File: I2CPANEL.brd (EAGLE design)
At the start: 54 x 83 mm, 47 parts, among them IC1 ATMEGA32U4-QFN

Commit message: Schematic and routing for v1.0 release
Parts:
- removed C1: 100nF 0603, freetronics-master-v1.1:0603
- removed C3, C4: 1uF 0603, freetronics-master-v1.1:0603
- removed C5, C6: 15pF 0603, freetronics-master-v1.1:0603
- removed F1: 500mA PTC 1812, rcl:L1812
- removed IC1: ATMEGA32U4-QFN, freetronics-jon:QFN-44N
- removed ICSP: ICSP, pinhead:2X03
- removed LED2: RED, freetronics-jon:LED-0603
- removed LED3: GREEN, freetronics-jon:LED-0603
- removed R1, R6: 22R, freetronics-jon:0603
- removed R18: 5.1K, freetronics-original:0603
- removed R2: 10K 0603, freetronics-master-v1.1:0603
- removed R4, R5: 1K, freetronics-jon:0603
- removed S10: 10, freetronics-original:TACTILE-PTH
- removed S11: 11, freetronics-original:TACTILE-PTH
- removed S12: 12, freetronics-original:TACTILE-PTH
- removed S13: 13, freetronics-original:TACTILE-PTH
- removed S14: 14, freetronics-original:TACTILE-PTH
- removed S15: 15, freetronics-original:TACTILE-PTH
- removed S16: 16, freetronics-original:TACTILE-PTH
- removed S17: 17, freetronics-original:TACTILE-PTH
- removed S18: 18, freetronics-original:TACTILE-PTH
- removed S19: 19, freetronics-original:TACTILE-PTH
- removed S20: 20, freetronics-original:TACTILE-PTH
- removed S21: RESET, freetronics-jon:TACTILE_SWITCH_SMD_2PIN_TINY
- removed S22: HWB, freetronics-jon:TACTILE_SWITCH_SMD_2PIN_TINY
- removed S7: 7, freetronics-original:TACTILE-PTH
- removed S8: 8, freetronics-original:TACTILE-PTH
- removed S9: 9, freetronics-original:TACTILE-PTH
- removed U$15: USB-C, freetronics-jon:USB-C-U52A
- removed XTL1: 16MHz, freetronics-jon:CRYSTAL-SMD-3X2
- removed Z1, Z2: PGB1010603, freetronics-master-v1.1:0603
- added IC2: MCP23017SO, microchip:SO28W
- added JP1: M100.1, freetronics-original:1X10
- added JP3: OLED, freetronics-jon:1X04
- added R27, R28: 4K7, freetronics-master-v1:0603
- added R29, R30, R31: 10K, freetronics-master-v1:0603
- added SJ2, SJ3, SJ4, SJ5: (no value), freetronics-jon:SJ
- C2: value 100nF 0603 -> 1uF
- SJ1: value HWB -> (none)
- moved LED1 99.4 mm to (72.5, 4.00)
- moved JP2 97.4 mm to (92.0, 19.0), flipped to the bottom
- moved R3 94.3 mm to (70.5, 4.00), turned to 90 degrees
- moved C2 87.0 mm to (88.0, 8.00)
- moved SJ1 67.3 mm to (56.0, 26.0), turned to 90 degrees
- moved S1 51.0 mm to (44.0, 15.0), flipped to the bottom
- moved S4 46.6 mm to (32.0, 8.00), flipped to the bottom
- moved S2 38.0 mm to (20.0, 15.0), flipped to the bottom
- moved S6 36.1 mm to (9.00, 8.00), flipped to the bottom
- moved S3 31.0 mm to (32.0, 22.0), flipped to the bottom
- moved S5 20.0 mm to (9.00, 22.0), flipped to the bottom
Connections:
- removed net 3V3: C4.2, IC1.6
- removed net 5V: C2.1, C3.1, F1.2, IC1.14, IC1.2, IC1.24, IC1.34, IC1.44, IC1.7, ICSP.2, JP2.3, R2.2, R3.2, R4.2, R5.2
- removed net A0: IC1.36
- removed net A1: IC1.37
- removed net A2: IC1.38
- removed net A3: IC1.39
- removed net A4: IC1.40
- removed net A5: IC1.41
- removed net AREF: C1.1, IC1.42
- removed net COL0: IC1.25, S1.1, S1.2, S13.1, S13.2, S17.1, S17.2, S5.1, S5.2, S9.1, S9.2
- removed net COL1: IC1.31, S10.1, S10.2, S14.1, S14.2, S18.1, S18.2, S2.1, S2.2, S6.1, S6.2
- removed net COL2: IC1.20, S11.1, S11.2, S15.1, S15.2, S19.1, S19.2, S3.1, S3.2, S7.1, S7.2
- removed net COL3: IC1.21, S12.1, S12.2, S16.1, S16.2, S20.1, S20.2, S4.1, S4.2, S8.1, S8.2
- removed net D+: R6.1, U$15.A6, U$15.B6, Z2.2
- removed net D-: R1.1, U$15.A7, U$15.B7, Z1.2
- removed net D11: IC1.12
- removed net D13: IC1.32
- removed net D2_SDA: IC1.19, JP2.1
- removed net D3_SCL: IC1.18, JP2.2
- removed net D7_AIN0: IC1.1
- removed net HWB: IC1.33, S22.1, SJ1.1
- removed net MISO: IC1.11, ICSP.1
- removed net MOSI: IC1.10, ICSP.4
- removed net N$11: C5.2, IC1.17, XTL1.3
- removed net N$12: C6.2, IC1.16, XTL1.1
- removed net N$67: R18.2, U$15.A5, U$15.B5
- removed net RD+: IC1.4, R6.2
- removed net RD-: IC1.3, R1.2
- removed net RESET: IC1.13, ICSP.5, R2.1, S21.2
- removed net ROW0: IC1.27, S1.3, S1.4, S2.3, S2.4, S3.3, S3.4, S4.3, S4.4
- removed net ROW1: IC1.26, S5.3, S5.4, S6.3, S6.4, S7.3, S7.4, S8.3, S8.4
- removed net ROW2: IC1.28, S10.3, S10.4, S11.3, S11.4, S12.3, S12.4, S9.3, S9.4
- removed net ROW3: IC1.29, S13.3, S13.4, S14.3, S14.4, S15.3, S15.4, S16.3, S16.4
- removed net ROW4: IC1.30, S17.3, S17.4, S18.3, S18.4, S19.3, S19.4, S20.3, S20.4
- removed net RXLED_SS: IC1.8, LED3.C
- removed net SCK: IC1.9, ICSP.3
- removed net TX_LED: IC1.22, LED2.C
- removed net USB+: F1.1, U$15.A4, U$15.A9, U$15.B4, U$15.B9
- new net ADDR0: IC2.15, R29.2, SJ1.1
- new net ADDR1: IC2.16, R30.2, SJ2.1
- new net ADDR2: IC2.17, R31.2, SJ3.1
- new net GPA1: IC2.22, S1.1, S1.2
- new net GPA2: IC2.23, S2.1, S2.2
- new net GPA3: IC2.24, S3.1, S3.2
- new net GPA4: IC2.25, S4.1, S4.2
- new net GPA5: IC2.26, S5.1, S5.2
- new net GPA6: IC2.27, S6.1, S6.2
- new net N$1: IC2.1, JP1.1
- new net N$2: IC2.2, JP1.2
- new net N$3: IC2.3, JP1.3
- new net N$4: IC2.4, JP1.4
- new net N$42: R27.2, SJ4.1
- new net N$43: R28.2, SJ5.1
- new net N$5: IC2.5, JP1.5
- new net N$9: IC2.8, JP1.8
- new net SCL: IC2.12, JP2.2, JP3.2, R27.1
- new net SDA: IC2.13, JP2.1, JP3.1, R28.1
- new net VCC: C2.1, IC2.18, IC2.9, JP1.9, JP2.3, JP3.3, R3.2, SJ1.2, SJ2.2, SJ3.2, SJ4.2, SJ5.2
- net GND: now also IC2.10, JP1.10, JP3.4, R29.1, R30.1, R31.1, S1.3, S1.4, S2.3, S2.4, S3.3, S3.4, S4.3, S4.4, S5.3, S5.4, S6.3, S6.4; no longer C1.2, C3.2, C4.1, C5.1, C6.1, IC1.15, IC1.23, IC1.35, IC1.43, IC1.5, IC1.TGND, ICSP.6, R18.1, S21.1, S22.2, SJ1.2, U$15.A1, U$15.A12, U$15.B1, U$15.B12, U$15.CASE1, U$15.CASE2, U$15.CASE3, U$15.CASE4, U$15.FIX1, U$15.FIX2, U$15.FIX3, U$15.FIX4, XTL1.2, XTL1.4, Z1.1, Z2.1
- net N$7: now also IC2.6, JP1.6; no longer LED2.A, R4.1
- net N$8: now also IC2.7, JP1.7; no longer LED3.A, R5.1
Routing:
- net ROW4: track 123.0 -> 0.00 mm
- net ROW3: track 111.5 -> 0.00 mm
- net 5V: track 111.1 -> 0.00 mm, vias 5 -> 0
- net ROW2: track 100.0 -> 0.00 mm
- net COL0: track 88.9 -> 0.00 mm, vias 1 -> 0
- net ROW1: track 88.6 -> 0.00 mm
- net COL1: track 86.0 -> 0.00 mm, vias 1 -> 0
- net ROW0: track 76.2 -> 0.00 mm, vias 1 -> 0
- net SDA: track 0.00 -> 68.0 mm, vias 0 -> 1
- net COL3: track 67.0 -> 0.00 mm
- net COL2: track 65.5 -> 0.00 mm
- net HWB: track 60.6 -> 0.00 mm, vias 2 -> 0
- net GPA5: track 0.00 -> 59.5 mm
- net SCL: track 0.00 -> 55.3 mm, vias 0 -> 1
- net GPA6: track 0.00 -> 53.0 mm
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- added copper zone on layer 1, net VCC
- removed copper zone on layer 1, net GND
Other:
- board size 54 x 83 mm -> 99 x 30 mm
- board text added: "0"
- board text added: "A0"
- board text added: "A1"
- board text added: "A2"
- board text added: "Copyright 2019 SuperHouse Automation Pty Ltd Released under the TAPR Open Hardware License www.tapr.org/OHL"
- board text added: "G"
- board text added: "GPA1"
- board text added: "GPA2"
- board text added: "GPA3"
- board text added: "GPA4"
- board text added: "GPA5"
- board text added: "GPA6"
- board text added: "GPB0-7"
- board text added: "I2C"
- board text added: "I2C Addresses: 0x20 MCP23017 0x3C 128x32 OLED"
- board text added: "I2C Control Panel"
- board text added: "Pullups"
- board text added: "SCL"
- board text added: "SDA"
- board text added: "V"
- board text added: "VIN"
- board text added: "VIN: 3.3-5V"
- board text added: "www.superhouse.tv/i2cpanel"
- board text removed: "10"
- board text removed: "11"
- board text removed: "12"
- board text removed: "13"
- board text removed: "14"
- board text removed: "15"
- board text removed: "16"
- board text removed: "17"
- board text removed: "18"
- board text removed: "19"
- board text removed: "20"
- board text removed: "8"
- board text removed: "9"
- board text removed: "Arduino Leonardo Compatible"
- board text removed: "Col0: D4 Col1: D5 Col2: D0 Col3: D1"
- board text removed: "Copyright 2018 SuperHouse Automation Pty Ltd Released under the TAPR Open Hardware License www.tapr.org/OHL"
- board text removed: "HWB"
- board text removed: "ICSP"
- board text removed: "LeoPad Mini"
- board text removed: "RST"
- board text removed: "Row0: D6 Row1: D12 Row2: D8 Row3: D9 Row4: D10"
- board text removed: "Rx"
- board text removed: "Tx"
- board text removed: "USB-C"
- board text removed: "www.superhouse.tv/lpmini"

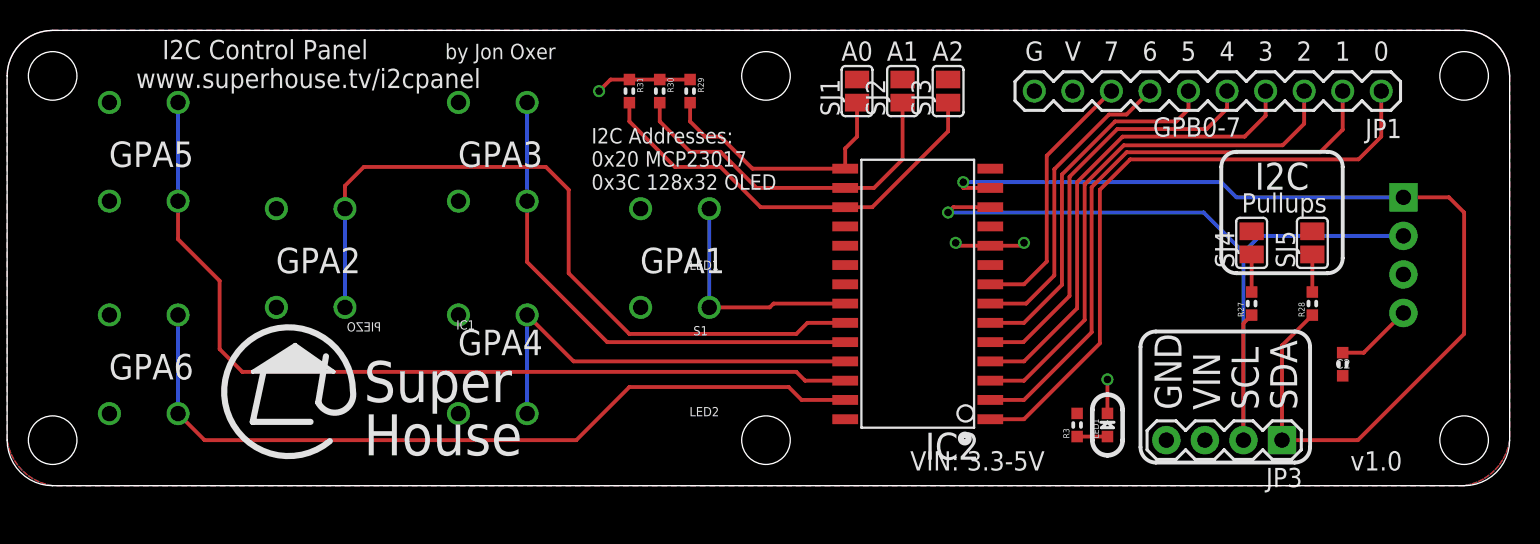
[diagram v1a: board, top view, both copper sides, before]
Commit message: Major rework to use 128x32 screen for v1.0 release
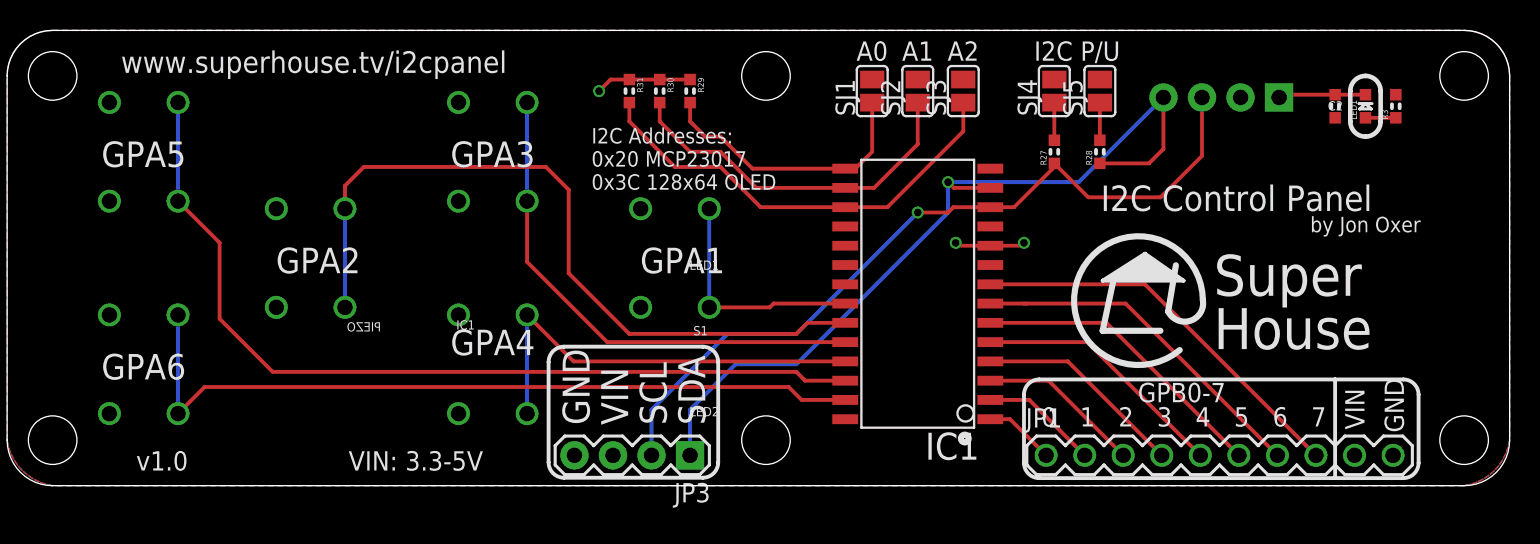
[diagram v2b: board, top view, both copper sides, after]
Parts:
- removed JP2: OLED, freetronics-jon:1X04
- added IC1: MCP23017SO, microchip:SO28W
- IC2: value MCP23017SO -> 128X64 OLED; device microchip:SO28W -> freetronics-jon:OLED-128X64
- moved JP3 39.0 mm to (45.0, 2.00)
- moved JP1 32.6 mm to (68.5, 2.00), turned to 0 degrees
- moved R3 29.7 mm to (91.5, 25.0)
- moved LED1 27.0 mm to (89.5, 25.0)
- moved IC2 20.2 mm to (80.0, 15.0), flipped to the bottom, turned to 0 degrees
- moved R28 17.2 mm to (72.0, 22.0)
- moved SJ5 17.2 mm to (72.0, 26.0)
- moved C2 17.0 mm to (87.5, 25.0)
- moved R27 16.4 mm to (69.0, 22.0)
- moved SJ4 16.4 mm to (69.0, 26.0)
- moved SJ1 1.00 mm to (57.0, 26.0)
- moved SJ2 1.00 mm to (60.0, 26.0)
- moved SJ3 1.00 mm to (63.0, 26.0)
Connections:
- net ADDR0: now also IC1.15; no longer IC2.15
- net ADDR1: now also IC1.16; no longer IC2.16
- net ADDR2: now also IC1.17; no longer IC2.17
- net GND: now also IC1.10, IC2.GND; no longer IC2.10, JP2.4
- net GPA1: now also IC1.22; no longer IC2.22
- net GPA2: now also IC1.23; no longer IC2.23
- net GPA3: now also IC1.24; no longer IC2.24
- net GPA4: now also IC1.25; no longer IC2.25
- net GPA5: now also IC1.26; no longer IC2.26
- net GPA6: now also IC1.27; no longer IC2.27
- net N$1: now also IC1.1; no longer IC2.1
- net N$2: now also IC1.2; no longer IC2.2
- net N$3: now also IC1.3; no longer IC2.3
- net N$4: now also IC1.4; no longer IC2.4
- net N$5: now also IC1.5; no longer IC2.5
- net N$7: now also IC1.6; no longer IC2.6
- net N$8: now also IC1.7; no longer IC2.7
- net N$9: now also IC1.8; no longer IC2.8
- net SCL: now also IC1.12, IC2.SCL; no longer IC2.12, JP2.2
- net SDA: now also IC1.13, IC2.SDA; no longer IC2.13, JP2.1
- net VCC: now also IC1.18, IC1.9, IC2.VCC; no longer IC2.18, IC2.9, JP2.3
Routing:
- net N$1: track 42.4 -> 4.67 mm
- net N$2: track 38.7 -> 7.73 mm
- net N$3: track 35.1 -> 10.8 mm
- net N$4: track 31.3 -> 13.9 mm
- net SDA: track 68.0 -> 54.8 mm
- net N$5: track 27.7 -> 16.9 mm
- net N$9: track 17.3 -> 26.1 mm
- net N$7: track 24.3 -> 20.0 mm
- net SCL: track 55.3 -> 52.0 mm
- net N$8: track 20.4 -> 23.1 mm
- net GND: track 18.3 -> 16.7 mm, vias 4 -> 3
- net GPA6: track 53.0 -> 51.5 mm
- net GPA5: track 59.5 -> 58.3 mm
- net ADDR2: track 28.5 -> 29.5 mm
- net ADDR0: track 17.4 -> 18.2 mm
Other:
- board text added: "I2C Addresses: 0x20 MCP23017 0x3C 128x64 OLED"
- board text added: "I2C P/U"
- board text removed: "5V"
- board text removed: "D2/SDA"
- board text removed: "D3/SCL"
- board text removed: "G"
- board text removed: "I2C"
- board text removed: "I2C Addresses: 0x20 MCP23017 0x3C 128x32 OLED"
- board text removed: "Pullups"
- board text removed: "V"

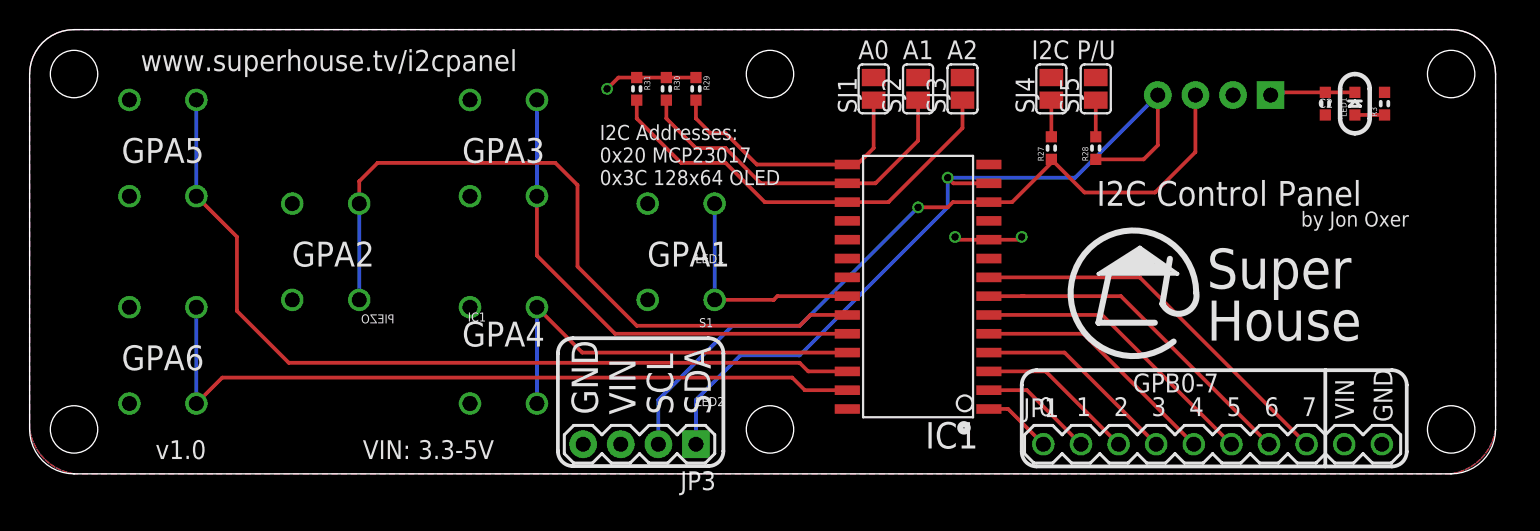
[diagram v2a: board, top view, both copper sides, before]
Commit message: Added mechanical dimensions
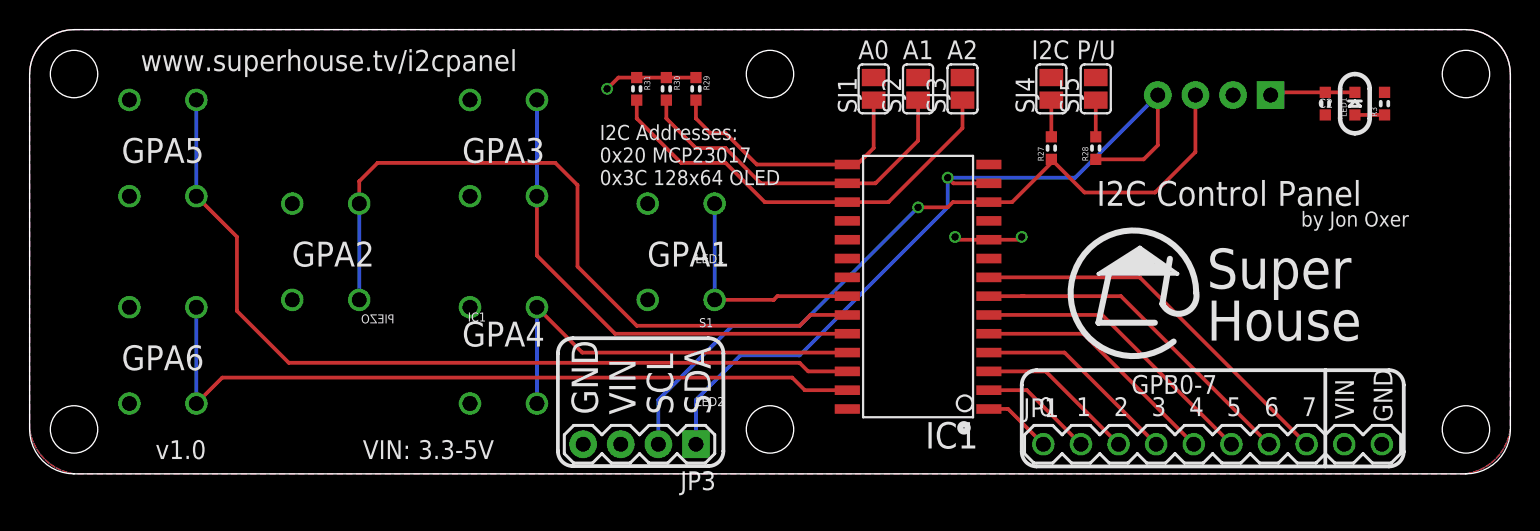
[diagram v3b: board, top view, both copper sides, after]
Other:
- board size 99 x 30 mm -> 100 x 30 mm
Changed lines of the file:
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@@
 <setting verticaltext="up"/>
 </settings>
-<grid distance="0.5" unitdist="mm" unit="mm" style="dots" multiple="1" display="yes" altdistance="0.001" altunitdist="inch" altunit="inch"/>
+<grid distance="1" unitdist="mm" unit="mm" style="dots" multiple="1" display="yes" altdistance="0.001" altunitdist="inch" altunit="inch"/>
 <layers>
 <layer number="1" name="Top" color="4" fill="1" visible="yes" active="yes"/>
@@
 <layer number="45" name="Holes" color="7" fill="1" visible="yes" active="yes"/>
 <layer number="46" name="Milling" color="3" fill="1" visible="no" active="yes"/>
-<layer number="47" name="Measures" color="7" fill="1" visible="no" active="yes"/>
+<layer number="47" name="Measures" color="7" fill="1" visible="yes" active="yes"/>
 <layer number="48" name="Document" color="7" fill="1" visible="no" active="yes"/>
 <layer number="49" name="Reference" color="7" fill="1" visible="no" active="yes"/>
@@
 <board>
 <plain>
-<wire x1="3" y1="0" x2="96" y2="0" width="0" layer="20"/>
-<wire x1="99" y1="3" x2="99" y2="27" width="0" layer="20"/>
-<wire x1="96" y1="30" x2="3" y2="30" width="0" layer="20"/>
+<wire x1="3" y1="0" x2="97" y2="0" width="0" layer="20"/>
+<wire x1="100" y1="3" x2="100" y2="27" width="0" layer="20"/>
+<wire x1="97" y1="30" x2="3" y2="30" width="0" layer="20"/>
 <wire x1="0" y1="3" x2="3" y2="0" width="0" layer="20" curve="90"/>
 <wire x1="0" y1="3" x2="0" y2="27" width="0" layer="20"/>
 <wire x1="0" y1="27" x2="3" y2="30" width="0" layer="20" curve="-90"/>
-<wire x1="96" y1="30" x2="99" y2="27" width="0" layer="20" curve="-90"/>
-<wire x1="96" y1="0" x2="99" y2="3" width="0" layer="20" curve="90"/>
+<wire x1="97" y1="30" x2="100" y2="27" width="0" layer="20" curve="-90"/>
+<wire x1="97" y1="0" x2="100" y2="3" width="0" layer="20" curve="90"/>
 <circle x="63.1" y="3.1064" radius="0.254" width="0.4064" layer="21"/>
 <text x="7.5" y="27.2" size="1.4224" layer="21" font="vector" ratio="17">www.superhouse.tv/i2cpanel</text>
@@
 <text x="8.5" y="1" size="1.27" layer="21" font="vector" ratio="15">v1.0</text>
 <hole x="3" y="27" drill="3.2"/>
-<hole x="96" y="27" drill="3.2"/>
+<hole x="97" y="27" drill="3.2"/>
 <text x="81" y="18.1" size="1.6764" layer="21" font="vector" ratio="18" align="bottom-center">I2C Control Panel</text>
 <hole x="3" y="3" drill="3.2"/>
-<hole x="96" y="3" drill="3.2"/>
+<hole x="97" y="3" drill="3.2"/>
 <text x="24.5" y="14" size="2.54" layer="22" font="vector" ratio="15" rot="MR0" align="bottom-center">2</text>
 <text x="48.5" y="14" size="2.54" layer="22" font="vector" ratio="15" rot="MR0" align="bottom-center">1</text>
@@
 0x20 MCP23017
 0x3C 128x64 OLED</text>
-<text x="74.5" y="5.5" size="1.27" layer="21" font="vector" ratio="15">GPB0-7</text>
+<text x="74.4" y="5.4" size="1.27" layer="21" font="vector" ratio="15">GPB0-7</text>
 <text x="22.5" y="1" size="1.27" layer="21" font="vector" ratio="15">VIN: 3.3-5V</text>
 <text x="70.5" y="28" size="1.27" layer="21" font="vector" ratio="16" align="bottom-center">I2C P/U</text>
 <wire x1="68" y1="7" x2="67" y2="6" width="0.254" layer="21" curve="90"/>
 <wire x1="68" y1="7" x2="87.5" y2="7" width="0.254" layer="21"/>
-<wire x1="87.5" y1="7" x2="92" y2="7" width="0.254" layer="21"/>
-<wire x1="92" y1="7" x2="93" y2="6" width="0.254" layer="21" curve="-90"/>
+<wire x1="87.5" y1="7" x2="91.8" y2="7" width="0.254" layer="21"/>
+<wire x1="91.8" y1="7" x2="92.8" y2="6" width="0.254" layer="21" curve="-90"/>
 <wire x1="87.5" y1="0.5" x2="87.5" y2="7" width="0.254" layer="21"/>
-<wire x1="68" y1="0.5" x2="92" y2="0.5" width="0.254" layer="21"/>
+<wire x1="68" y1="0.5" x2="91.8" y2="0.5" width="0.254" layer="21"/>
 <wire x1="68" y1="0.5" x2="67" y2="1.5" width="0.254" layer="21" curve="-90"/>
 <wire x1="67" y1="1.5" x2="67" y2="6" width="0.254" layer="21"/>
-<wire x1="92" y1="0.5" x2="93" y2="1.5" width="0.254" layer="21" curve="90"/>
-<wire x1="93" y1="1.5" x2="93" y2="6" width="0.254" layer="21"/>
+<wire x1="91.8" y1="0.5" x2="92.8" y2="1.5" width="0.254" layer="21" curve="90"/>
+<wire x1="92.8" y1="1.5" x2="92.8" y2="6" width="0.254" layer="21"/>
+<dimension x1="0" y1="30" x2="100" y2="30" x3="50" y3="37" textsize="1.778" layer="47" precision="0" visible="yes"/>
+<dimension x1="100" y1="0" x2="100" y2="30" x3="109" y3="15" textsize="1.778" layer="47" precision="0" visible="yes"/>
+<dimension x1="99" y1="27" x2="99" y2="3" x3="106" y3="15" textsize="1.778" layer="47" dtype="diameter" precision="0" visible="yes"/>
+<dimension x1="3" y1="29" x2="50" y2="29" x3="26.5" y3="32" textsize="1.778" layer="47" dtype="horizontal" precision="0" visible="yes"/>
+<dimension x1="50" y1="29" x2="97" y2="29" x3="73.5" y3="32" textsize="1.778" layer="47" dtype="horizontal" precision="0" visible="yes"/>
+<dimension x1="3" y1="29" x2="0" y2="34" x3="1.5" y3="34" textsize="1.778" layer="47" dtype="horizontal" precision="0" visible="yes"/>
+<dimension x1="99" y1="3" x2="102" y2="0" x3="103" y3="1.5" textsize="1.778" layer="47" dtype="vertical" precision="0" visible="yes"/>
+<dimension x1="93" y1="9" x2="93" y2="21" x3="97" y3="15" textsize="1.778" layer="47" dtype="vertical" precision="0" visible="yes"/>
+<dimension x1="68" y1="-1" x2="92" y2="-1" x3="80" y3="-3" textsize="1.778" layer="47" dtype="horizontal" precision="0" visible="yes"/>
+<dimension x1="68" y1="-1" x2="44" y2="-1" x3="56" y3="-3" textsize="1.778" layer="47" dtype="horizontal" precision="0" visible="yes"/>
+<dimension x1="44" y1="-1" x2="32" y2="-1" x3="38" y3="-3" textsize="1.778" layer="47" dtype="horizontal" precision="0" visible="yes"/>
+<dimension x1="32" y1="-1" x2="20" y2="-1" x3="26" y3="-3" textsize="1.778" layer="47" dtype="horizontal" precision="0" visible="yes"/>
+<dimension x1="20" y1="-1" x2="9" y2="-1" x3="14.5" y3="-3" textsize="1.778" layer="47" dtype="horizontal" precision="0" visible="yes"/>
+<dimension x1="9" y1="-1" x2="0" y2="-1" x3="4.5" y3="-3" textsize="1.778" layer="47" dtype="horizontal" precision="0" visible="yes"/>
+<dimension x1="92" y1="-1" x2="100" y2="-1" x3="96" y3="-3" textsize="1.778" layer="47" dtype="horizontal" precision="0" visible="yes"/>
+<dimension x1="5" y1="8" x2="5" y2="22" x3="-2" y3="15" textsize="1.778" layer="47" dtype="vertical" precision="0" visible="yes"/>
+<dimension x1="-1" y1="0" x2="-1" y2="8" x3="-2" y3="4" textsize="1.778" layer="47" dtype="vertical" precision="0" visible="yes"/>
+<dimension x1="-1" y1="22" x2="-1" y2="30" x3="-2" y3="26" textsize="1.778" layer="47" dtype="vertical" precision="0" visible="yes"/>
 </plain>
 <attributes>
@@
 <vertex x="0" y="27" curve="-90"/>
 <vertex x="3" y="30"/>
-<vertex x="96" y="30" curve="-90"/>
-<vertex x="99" y="27"/>
-<vertex x="99" y="3" curve="-73.73763"/>
-<vertex x="96" y="0"/>
+<vertex x="97" y="30" curve="-90"/>
+<vertex x="100" y="27"/>
+<vertex x="100" y="3" curve="-73.73763"/>
+<vertex x="97" y="0"/>
 <vertex x="3" y="0" curve="-73.73763"/>
 <vertex x="0" y="3"/>
@@
 <vertex x="0" y="27" curve="-90"/>
 <vertex x="3" y="30"/>
-<vertex x="96" y="30" curve="-90"/>
-<vertex x="99" y="27"/>
-<vertex x="99" y="3" curve="-73.73763"/>
-<vertex x="96" y="0"/>
+<vertex x="97" y="30" curve="-90"/>
+<vertex x="100" y="27"/>
+<vertex x="100" y="3" curve="-73.73763"/>
+<vertex x="97" y="0"/>
 <vertex x="3" y="0" curve="-73.73763"/>
 <vertex x="0" y="3"/>
